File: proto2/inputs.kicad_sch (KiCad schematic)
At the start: 12 parts, among them U19 EL817, U20 EL817, U21 EL817, U22 EL817

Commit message: Laying out board. in-process commit.
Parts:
- added F16, F17: 0.1A, Resistor_SMD:R_0805_2012Metric, symbol Device:Polyfuse
- U19, U20, U21, U22: value EL817 -> EL817S1; footprint Package_SO:SO-4_7.6x3.6mm_P2.54mm -> JLCPCB:SO-4_6.5x4.8mm_P2.54mm; symbol Isolator:EL817 -> JLCPCB:EL817S1
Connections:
- new net +24V: F16.2, F17.2
- new net 24V_DI1: F16.1
- new net 24V_DI2: F17.1

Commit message: Final layout for 0.2.0 and various BOM and minor schematic updates.
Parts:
- F16, F17: footprint Resistor_SMD:R_0805_2012Metric -> Resistor_SMD:R_1206_3216Metric; LCSC (none) -> C70065
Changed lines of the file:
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@@
     (property "Reference" "F17" (id 0) (at 179.07 60.325 90))
     (property "Value" "0.1A" (id 1) (at 179.07 62.6364 90))
-    (property "Footprint" "Resistor_SMD:R_0805_2012Metric" (id 2) (at 173.99 67.31 0)
+    (property "Footprint" "Resistor_SMD:R_1206_3216Metric" (id 2) (at 173.99 67.31 0)
       (effects (font (size 1.27 1.27)) (justify left) hide)
     )
-    (property "Datasheet" "" (id 3) (at 179.07 66.04 0)
+    (property "Datasheet" "https://datasheet.lcsc.com/lcsc/1811091410_TECHFUSE-nSMD010_C70065.pdf" (id 3) (at 179.07 66.04 0)
       (effects (font (size 1.27 1.27)) hide)
     )
-    (property "LCSC" "" (id 4) (at 179.07 66.04 0)
+    (property "LCSC" "C70065" (id 4) (at 179.07 66.04 0)
       (effects (font (size 1.27 1.27)) hide)
     )
@@
     (property "Reference" "F16" (id 0) (at 179.07 40.005 90))
     (property "Value" "0.1A" (id 1) (at 179.07 42.3164 90))
-    (property "Footprint" "Resistor_SMD:R_0805_2012Metric" (id 2) (at 173.99 46.99 0)
+    (property "Footprint" "Resistor_SMD:R_1206_3216Metric" (id 2) (at 173.99 46.99 0)
       (effects (font (size 1.27 1.27)) (justify left) hide)
     )
-    (property "Datasheet" "" (id 3) (at 179.07 45.72 0)
+    (property "Datasheet" "https://datasheet.lcsc.com/lcsc/1811091410_TECHFUSE-nSMD010_C70065.pdf" (id 3) (at 179.07 45.72 0)
       (effects (font (size 1.27 1.27)) hide)
     )
-    (property "LCSC" "" (id 4) (at 179.07 45.72 0)
+    (property "LCSC" "C70065" (id 4) (at 179.07 45.72 0)
       (effects (font (size 1.27 1.27)) hide)
     )

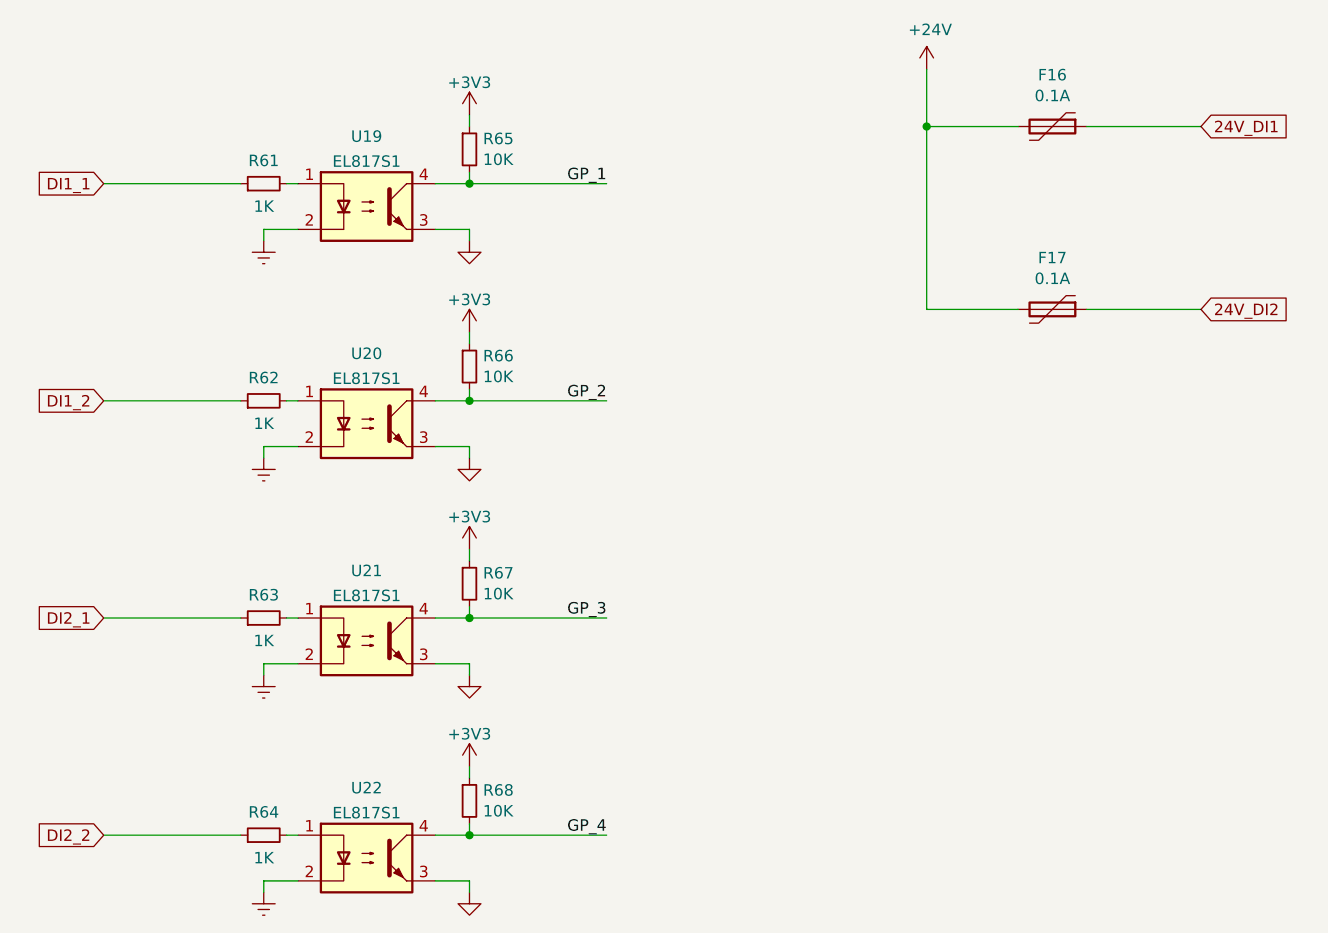
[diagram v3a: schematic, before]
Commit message: Rearranged GPIO around the boot pins.
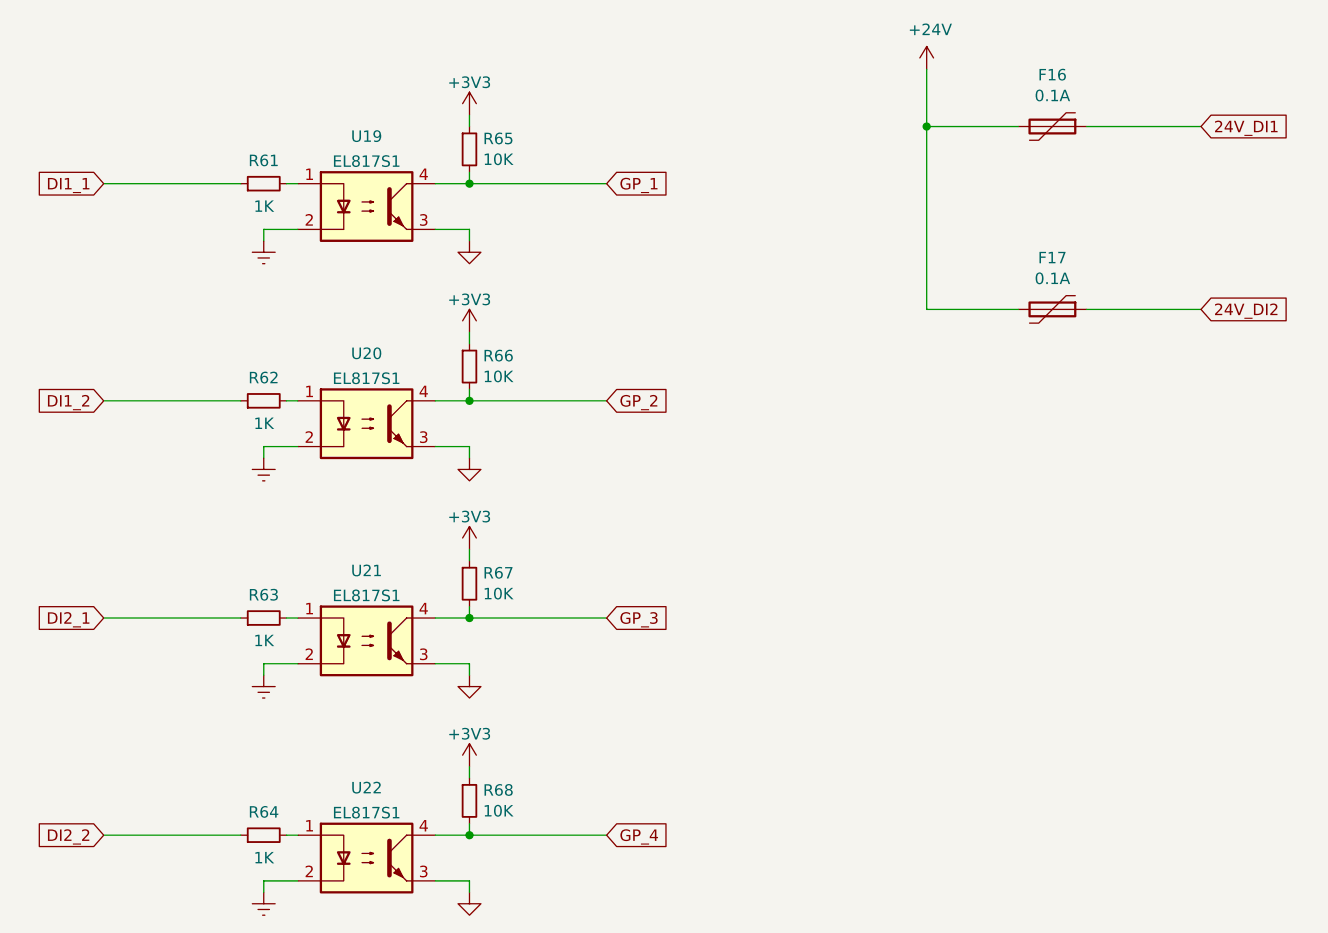
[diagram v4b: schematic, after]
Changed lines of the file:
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@@
   (title_block
     (title "Greenhouse 2.0 IO Board")
-    (date "2022-03-06")
-    (rev "0.2.0")
+    (date "2022-05-30")
+    (rev "0.2.1")
     (company "Langhe Greenhaus")
+    (comment 1 "Langhe Part Number: 240000")
   )
   (junction (at 114.3 124.46) (diameter 0) (color 0 0 0 0)
@@
     (stroke (width 0) (type default) (color 0 0 0 0))
   )
-  (label "GP_2" (at 129.54 76.2 180)
-    (effects (font (size 1.27 1.27)) (justify right bottom))
-  )
-  (label "GP_3" (at 129.54 100.33 180)
-    (effects (font (size 1.27 1.27)) (justify right bottom))
-  )
-  (label "GP_4" (at 129.54 124.46 180)
-    (effects (font (size 1.27 1.27)) (justify right bottom))
-  )
-  (label "GP_1" (at 129.54 52.07 180)
-    (effects (font (size 1.27 1.27)) (justify right bottom))
-  )
   (global_label "DI1_1" (shape input) (at 73.66 52.07 180) (fields_autoplaced)
     (effects (font (size 1.27 1.27)) (justify right))
@@
     )
   )
+  (global_label "GP_3" (shape input) (at 129.54 100.33 0) (fields_autoplaced)
+    (effects (font (size 1.27 1.27)) (justify left))
+    (property "Intersheet References" "${INTERSHEET_REFS}" (id 0) (at 136.5813 100.2506 0)
+      (effects (font (size 1.27 1.27)) (justify left) hide)
+    )
+  )
   (global_label "24V_DI1" (shape input) (at 195.58 45.72 0) (fields_autoplaced)
     (effects (font (size 1.27 1.27)) (justify left))
@@
     )
   )
+  (global_label "GP_2" (shape input) (at 129.54 76.2 0) (fields_autoplaced)
+    (effects (font (size 1.27 1.27)) (justify left))
+    (property "Intersheet References" "${INTERSHEET_REFS}" (id 0) (at 136.5813 76.1206 0)
+      (effects (font (size 1.27 1.27)) (justify left) hide)
+    )
+  )
   (global_label "DI2_2" (shape input) (at 73.66 124.46 180) (fields_autoplaced)
     (effects (font (size 1.27 1.27)) (justify right))
@@
     )
   )
+  (global_label "GP_1" (shape input) (at 129.54 52.07 0) (fields_autoplaced)
+    (effects (font (size 1.27 1.27)) (justify left))
+    (property "Intersheet References" "${INTERSHEET_REFS}" (id 0) (at 136.5813 51.9906 0)
+      (effects (font (size 1.27 1.27)) (justify left) hide)
+    )
+  )
   (global_label "DI1_2" (shape input) (at 73.66 76.2 180) (fields_autoplaced)
     (effects (font (size 1.27 1.27)) (justify right))
@@
     )
   )
+  (global_label "GP_4" (shape input) (at 129.54 124.46 0) (fields_autoplaced)
+    (effects (font (size 1.27 1.27)) (justify left))
+    (property "Intersheet References" "${INTERSHEET_REFS}" (id 0) (at 136.5813 124.3806 0)
+      (effects (font (size 1.27 1.27)) (justify left) hide)
+    )
+  )
